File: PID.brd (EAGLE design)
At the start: 160 x 100 mm, 11 parts, among them IC1 UA741CPE4, IC2 UA741CPE4, IC3 UA741CPE4

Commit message: paf
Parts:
- added CONSIGNE, RETOUR, RETOUR1: (no value), pinhead:1X01
- added IC4, IC5: UA741CPE4, SamacSys_Parts:DIP794W53P254L959H508Q8N
- added R1, R3, R4, R6: 22k, rcl:0204/7
- added R10, R7, R8, R9: 10k, rcl:0204/7
- added R11: 2.5k, rcl:0204/7
- added R5: (no value), rcl:0204/7
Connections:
- new net CONSIGNE: CONSIGNE.1, R4.1
- new net N$13: IC5.3, R4.2, R6.2
- new net N$15: IC4.2, R10.1, R7.2, R8.2, R9.2
- new net N$17: C3.+, R5.2
- new net N$18: IC4.3, R11.2
- new net N$9: IC5.2, R1.1, R3.2
- new net OUTPUT: IC4.6, R10.2, RETOUR1.1
- new net RETOUR: R3.1, R5.1, RETOUR.1
- net GND: now also R11.1, R6.1
- net N$10: now also R9.1
- net N$2: now also R7.1
- net N$4: now also R8.1
- net N$7: now also IC5.6, R1.2, R2.1
- net V+: now also IC4.7, IC5.7
- net V-: now also IC4.4, IC5.4

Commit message: paf
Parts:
- removed R5: (no value), rcl:0204/7
- removed VR1: T7YA103MT20, PFE:T7YA
- added R13, R14: 22k, rcl:0204/7
- R1, R3: value 22k -> (none)
- R11: value 2.5k -> 5k
- R2: value (none) -> T7YA103MT20; device rcl:0204/7 -> PFE:T7YA
- moved R1 112.5 mm to (-17.8, 22.9)
- moved R3 20.3 mm to (-30.5, -114.3)
- moved R2 9.92 mm to (-24.1, 15.2)
- renumbered C1 to CI1, C2 to CI2, C3 to CD1, C4 to CD2, VR2 to RI, VR3 to RD
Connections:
- new net N$16: IC4.2, R10.1, R7.2, R8.2
- net N$15: now also IC5.6, R13.2; no longer IC4.2, R10.1, R7.2, R8.2, R9.2
- net N$17: now also R3.2; no longer R5.2
- net N$18: now also R9.2
- net N$2: now also R2.C; no longer VR1.C
- net N$3: now also R1.2, R2.A, R2.B; no longer R2.2, VR1.A, VR1.B
- net N$7: now also R1.1; no longer IC5.6, R1.2, R2.1
- net N$9: now also R13.1, R14.2; no longer R1.1, R3.2
- net RETOUR: now also R14.1; no longer R5.1

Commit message: paf
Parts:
- renumbered RETOUR1 to OUTPUT
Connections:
- removed net N$7 (its old number): R1.1, RI.A, RI.B
- net N$15: now also R1.1, RI.A, RI.B
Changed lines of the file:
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@@
 <attribute name="VALUE" x="-32.1056" y="-156.6926" size="0.9906" layer="27" ratio="10"/>
 </element>
-<element name="RETOUR1" library="pinhead" library_urn="urn:adsk.eagle:library:325" package="1X01" package3d_urn="urn:adsk.eagle:package:22485/2" value="" x="-33.02" y="-161.29" smashed="yes">
+<element name="OUTPUT" library="pinhead" library_urn="urn:adsk.eagle:library:325" package="1X01" package3d_urn="urn:adsk.eagle:package:22485/2" value="" x="-33.02" y="-161.29" smashed="yes">
 <attribute name="NAME" x="-34.3662" y="-159.4612" size="1.27" layer="25" ratio="10"/>
 <attribute name="POPULARITY" value="64" x="-33.02" y="-161.29" size="1.778" layer="27" display="off"/>
@@
 <wire x1="-14.13" y1="-7.62" x2="-29.21" y2="-13.97" width="0" layer="19" extent="1-1"/>
 </signal>
-<signal name="N$7">
-<contactref element="RI" pad="A"/>
-<contactref element="RI" pad="B"/>
-<contactref element="R1" pad="1"/>
-<wire x1="-31.75" y1="-16.51" x2="-29.21" y2="-19.05" width="0" layer="19" extent="1-1"/>
-<wire x1="-21.59" y1="22.86" x2="-31.75" y2="-16.51" width="0" layer="19" extent="1-1"/>
-</signal>
 <signal name="N$8">
 <contactref element="CI1" pad="-"/>
@@
 <contactref element="IC4" pad="6"/>
 <contactref element="R10" pad="2"/>
-<contactref element="RETOUR1" pad="1"/>
+<contactref element="OUTPUT" pad="1"/>
 <wire x1="-26.67" y1="-151.13" x2="-33.02" y2="-161.29" width="0" layer="19" extent="1-1"/>
 <wire x1="-25.24" y1="-143.51" x2="-26.67" y2="-151.13" width="0" layer="19" extent="1-1"/>
@@
 <wire x1="-26.67" y1="-134.62" x2="-33.18" y2="-143.51" width="0" layer="19" extent="1-1"/>
 </signal>
-<signal name="N$16">
+<signal name="N$15">
+<contactref element="IC5" pad="6"/>
+<contactref element="R13" pad="2"/>
+<contactref element="RI" pad="A"/>
+<contactref element="RI" pad="B"/>
+<contactref element="R1" pad="1"/>
+<wire x1="-25.24" y1="-81.28" x2="-26.67" y2="-88.9" width="0" layer="19" extent="1-1"/>
+<wire x1="-29.21" y1="-19.05" x2="-25.24" y2="-81.28" width="0" layer="19" extent="1-1"/>
+<wire x1="-31.75" y1="-16.51" x2="-29.21" y2="-19.05" width="0" layer="19" extent="1-1"/>
+<wire x1="-21.59" y1="22.86" x2="-31.75" y2="-16.51" width="0" layer="19" extent="1-1"/>
+</signal>
+<signal name="N$7">
 <contactref element="R8" pad="2"/>
 <contactref element="R7" pad="2"/>
@@
 <wire x1="-26.67" y1="-124.46" x2="-26.67" y2="-129.54" width="0" layer="19" extent="1-1"/>
 </signal>
-<signal name="N$15">
-<contactref element="IC5" pad="6"/>
-<contactref element="R13" pad="2"/>
-<wire x1="-25.24" y1="-81.28" x2="-26.67" y2="-88.9" width="0" layer="19" extent="1-1"/>
-</signal>
 </signals>

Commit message: paf
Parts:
- moved CI1 1.27 mm to (-33.0, -24.1)
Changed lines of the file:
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@@
 <attribute name="VALUE" x="-29.493" y="-16.535" size="1.27" layer="27" align="center"/>
 </element>
-<element name="CI1" library="rcl" library_urn="urn:adsk.eagle:library:334" package="E2,5-6" package3d_urn="urn:adsk.eagle:package:23349/1" value="" x="-33.02" y="-25.4" smashed="yes">
-<attribute name="NAME" x="-30.353" y="-23.876" size="1.27" layer="25" ratio="10"/>
-<attribute name="POPULARITY" value="26" x="-33.02" y="-25.4" size="1.778" layer="27" display="off"/>
-<attribute name="SPICEPREFIX" value="C" x="-33.02" y="-25.4" size="1.778" layer="27" display="off"/>
-<attribute name="VALUE" x="-30.353" y="-28.067" size="1.27" layer="27" ratio="10"/>
+<element name="CI1" library="rcl" library_urn="urn:adsk.eagle:library:334" package="E2,5-6" package3d_urn="urn:adsk.eagle:package:23349/1" value="" x="-33.02" y="-24.13" smashed="yes">
+<attribute name="NAME" x="-30.353" y="-22.606" size="1.27" layer="25" ratio="10"/>
+<attribute name="POPULARITY" value="26" x="-33.02" y="-24.13" size="1.778" layer="27" display="off"/>
+<attribute name="SPICEPREFIX" value="C" x="-33.02" y="-24.13" size="1.778" layer="27" display="off"/>
+<attribute name="VALUE" x="-30.353" y="-26.797" size="1.27" layer="27" ratio="10"/>
 </element>
 <element name="CI2" library="rcl" library_urn="urn:adsk.eagle:library:334" package="E2,5-6" package3d_urn="urn:adsk.eagle:package:23349/1" value="" x="-33.02" y="-31.75" smashed="yes">
@@
 <contactref element="RI" pad="C"/>
 <contactref element="CI1" pad="+"/>
-<wire x1="-29.21" y1="-13.97" x2="-34.29" y2="-25.4" width="0" layer="19" extent="1-1"/>
+<wire x1="-29.21" y1="-13.97" x2="-34.29" y2="-24.13" width="0" layer="19" extent="1-1"/>
 <wire x1="-14.13" y1="-7.62" x2="-29.21" y2="-13.97" width="0" layer="19" extent="1-1"/>
 </signal>
@@
 <contactref element="CI1" pad="-"/>
 <contactref element="CI2" pad="-"/>
-<wire x1="-31.75" y1="-25.4" x2="-31.75" y2="-31.75" width="0" layer="19" extent="1-1"/>
+<wire x1="-31.75" y1="-24.13" x2="-31.75" y2="-31.75" width="0" layer="19" extent="1-1"/>
 </signal>
 <signal name="N$10">

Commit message: paf
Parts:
- removed R1, R3: (no value), rcl:0204/7
- removed R2: T7YA103MT20, PFE:T7YA
- added GND, V+, V-: (no value), pinhead:1X01
- added RD1, RP1: (no value), rcl:0204/7
- added RP: T7YA103MT20, PFE:T7YA
- added S1, S2, S3: TL36PO, switch:TL3XPO
- moved R10 197.1 mm to (57.1, 25.4)
- moved OUTPUT 190.4 mm to (57.1, 6.35)
- moved R11 188.6 mm to (58.4, 10.2)
- moved IC4 182.4 mm to (58.4, 17.8)
- moved R7 173.8 mm to (50.8, 29.2), turned to 270 degrees
- moved R8 169.4 mm to (50.8, 19.1), turned to 90 degrees
- moved R9 164.9 mm to (50.8, 8.89), turned to 90 degrees
- moved R6 148.8 mm to (8.89, 24.1), turned to 180 degrees
- moved RETOUR 148.6 mm to (10.2, 33.0), turned to 270 degrees
- moved CONSIGNE 143.1 mm to (7.62, 33.0), turned to 270 degrees
- moved R4 134.2 mm to (8.89, 29.2), turned to 180 degrees
- moved R14 126.9 mm to (8.89, 26.7), turned to 180 degrees
- moved R13 105.4 mm to (8.89, 8.89)
- moved IC5 103.8 mm to (8.89, 16.5)
- moved CD1 89.0 mm to (26.7, 6.35), turned to 90 degrees
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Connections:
- new net N$12: R7.1, S1.2
- new net N$16: R8.1, S2.2
- new net N$19: R9.1, S3.2
- net GND: now also GND.1, S1.1, S2.1, S3.1
- net N$10: now also S3.3; no longer R9.1
- net N$15: now also RP1.1; no longer R1.1
- net N$17: now also RD1.2; no longer R3.2
- net N$2: now also RP.C, S1.3; no longer R2.C, R7.1
- net N$3: now also RP.A, RP.B, RP1.2; no longer R1.2, R2.A, R2.B
- net N$4: now also S2.3; no longer R8.1
- net RETOUR: now also RD1.1; no longer R3.1
- net V+: now also V+.1
- net V-: now also V-.1
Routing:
- net V-: track 0.00 -> 136.0 mm
- net GND: track 0.00 -> 121.4 mm
- net V+: track 0.00 -> 109.3 mm
- net N$2: track 0.00 -> 38.8 mm
- net N$10: track 0.00 -> 35.4 mm
- net N$15: track 0.00 -> 33.5 mm
- net RETOUR: track 0.00 -> 31.3 mm
- net OUTPUT: track 0.00 -> 23.4 mm
- net N$4: track 0.00 -> 22.7 mm
- net N$9: track 0.00 -> 21.9 mm
- net N$11: track 0.00 -> 18.8 mm
- net N$13: track 0.00 -> 18.7 mm
- net N$18: track 0.00 -> 18.6 mm
- net N$3: track 0.00 -> 17.7 mm
- net N$17: track 0.00 -> 14.5 mm
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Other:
- board size 160 x 100 mm -> 67.3 x 40.3 mm

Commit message: couocu
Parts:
- removed S1, S2, S3: TL36PO, switch:TL3XPO
- added JP1, JP2, JP3: (no value), pinhead:1X02
- added R1: 100k, rcl:0204/7
- moved RP1 2.54 mm to (16.5, 33.0)
- moved IC4 1.80 mm to (57.1, 19.1)
- moved GND 1.80 mm to (55.9, 33.0)
- moved V- 1.80 mm to (53.3, 35.6)
- moved R7 1.80 mm to (49.5, 30.5)
- moved R8 1.80 mm to (49.5, 20.3)
- moved R9 1.80 mm to (49.5, 10.2)
- moved V+ 1.80 mm to (58.4, 30.5)
- moved R10 1.27 mm to (57.1, 26.7)
- moved R11 1.27 mm to (57.1, 10.2)
- moved CONSIGNE 1.27 mm to (6.35, 33.0)
- moved IC5 1.27 mm to (7.62, 16.5)
- moved R13 1.27 mm to (7.62, 8.89)
- moved R14 1.27 mm to (7.62, 26.7)
- moved R4 1.27 mm to (7.62, 29.2)
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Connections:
- net N$15 renamed ERREUR
- net GND: no longer S1.1, S2.1, S3.1
- net N$10: now also JP3.1; no longer S3.3
- net N$12: now also JP1.2; no longer S1.2
- net N$16: now also JP2.2; no longer S2.2
- net N$19: now also JP3.2; no longer S3.2
- net N$2: now also JP1.1; no longer S1.3
- net N$4: now also JP2.1, R1.2; no longer S2.3
- net N$5: now also R1.1
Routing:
- net V-: track 136.0 -> 111.5 mm
- net N$5: track 11.6 -> 27.6 mm
- net V+: track 109.3 -> 101.7 mm
- net N$10: track 35.4 -> 28.5 mm
- net N$4: track 22.7 -> 26.8 mm
- net N$2: track 38.8 -> 34.8 mm
- net N$3: track 17.7 -> 20.5 mm
- net N$18: track 18.6 -> 16.3 mm
- net N$16: track 7.81 -> 6.13 mm
- net N$9: track 21.9 -> 23.6 mm
- net N$19: track 6.66 -> 5.08 mm
- net N$7: track 10.6 -> 11.9 mm
- net N$11: track 18.8 -> 20.0 mm
- net N$17: track 14.5 -> 15.8 mm
- net ERREUR: track 33.5 -> 32.4 mm
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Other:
- board size 67.3 x 40.3 mm -> 70 x 44 mm
- board text added: "PID board alpha DX+"

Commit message: paf
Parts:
- added R2: 1k, rcl:0204/7
- CD1, CD2: value (none) -> 10µ
- CI1, CI2: value (none) -> 470µ
- RD, RP: value T7YA103MT20 -> 10k
- RD1: value (none) -> 200
- RI: value T7YA103MT20 -> 100k
- RP1: value (none) -> 1k
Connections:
- new net N$15: R2.2, RI.A, RI.B
- net ERREUR: now also R2.1; no longer RI.A, RI.B
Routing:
- net GND: track 121.1 -> 0.00 mm
- net V-: track 111.5 -> 0.00 mm
- net V+: track 101.7 -> 0.00 mm
- net N$2: track 34.8 -> 0.00 mm
- net ERREUR: track 32.4 -> 0.00 mm
- net RETOUR: track 31.9 -> 0.00 mm
- net N$10: track 28.5 -> 0.00 mm
- net N$5: track 27.6 -> 0.00 mm
- net N$4: track 26.8 -> 0.00 mm
- net OUTPUT: track 24.4 -> 0.00 mm
- net N$9: track 23.6 -> 0.00 mm
- net N$3: track 20.5 -> 0.00 mm
- net N$11: track 20.0 -> 0.00 mm
- net N$13: track 18.6 -> 0.00 mm
- net N$18: track 16.3 -> 0.00 mm
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
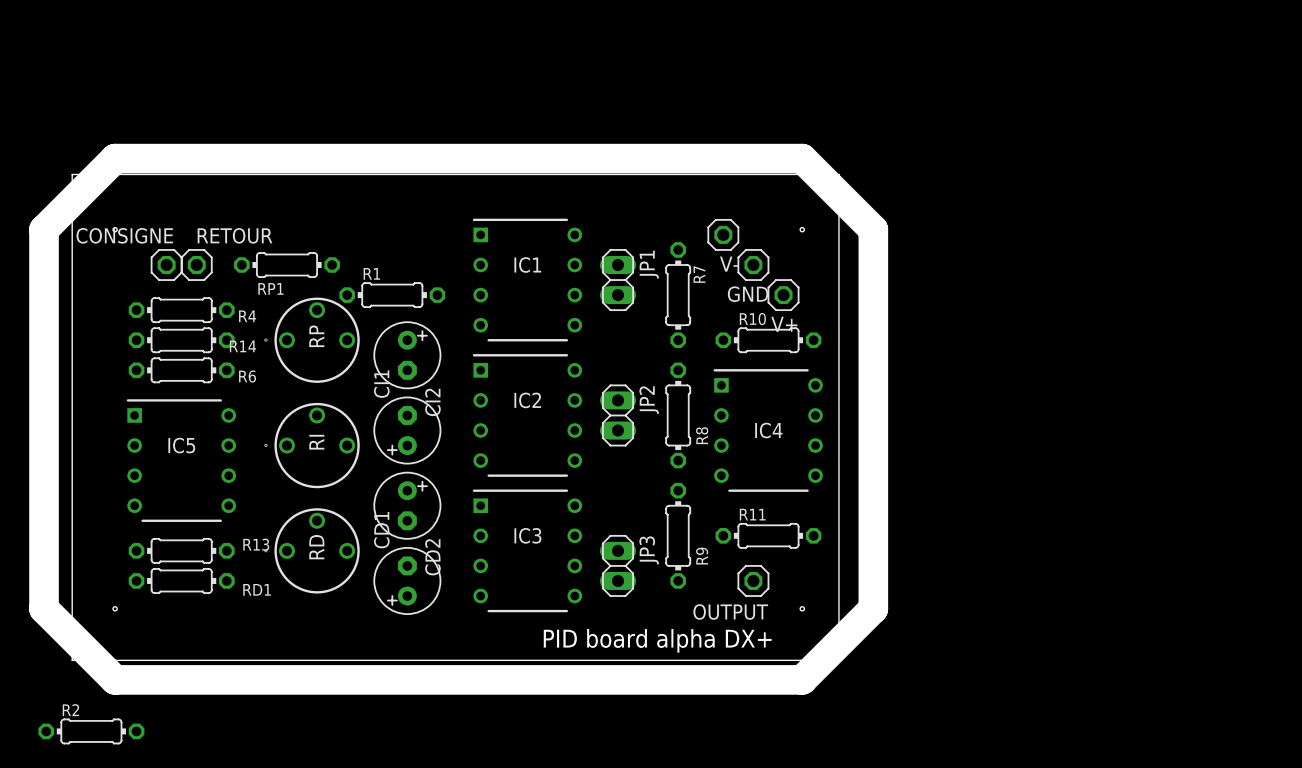
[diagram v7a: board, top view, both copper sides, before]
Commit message: Le routage de lavage, tous les signaux sur le bottom, le plan de masse sur le bottom, plan de V- sur le top et routage du V+ sur le top
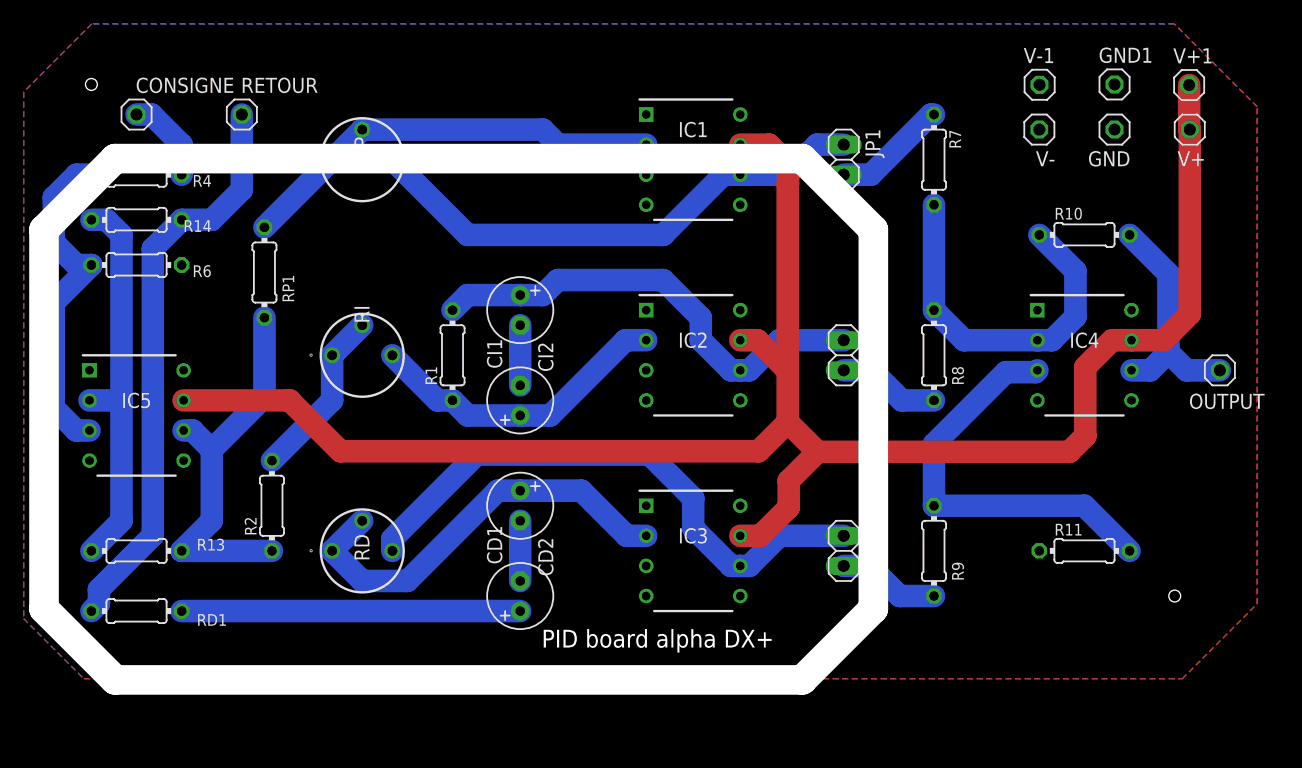
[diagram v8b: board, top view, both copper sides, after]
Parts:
- added GND1, V+1, V-1: (no value), pinhead:1X01
- moved OUTPUT 43.2 mm to (95.2, 24.1)
- moved V+ 37.0 mm to (92.7, 44.5)
- moved GND 32.6 mm to (86.4, 44.5)
- moved V- 28.1 mm to (80.0, 44.5)
- moved R10 28.1 mm to (83.8, 35.6)
- moved IC4 27.4 mm to (83.8, 25.4)
- moved R11 26.7 mm to (83.8, 8.89)
- moved R7 24.4 mm to (71.1, 41.9)
- moved R2 24.4 mm to (15.2, 12.7), turned to 90 degrees
- moved R8 22.2 mm to (71.1, 25.4)
- moved R9 21.6 mm to (71.1, 8.89)
- moved JP1 21.6 mm to (63.5, 41.9)
- moved JP2 19.7 mm to (63.5, 25.4)
- moved JP3 19.1 mm to (63.5, 8.89)
- moved IC1 17.3 mm to (50.8, 41.9)
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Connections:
- net GND: now also GND1.1
- net V+: now also V+1.1
- net V-: now also V-1.1
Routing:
- net V+: track 0.00 -> 158.7 mm
- net RETOUR: track 0.00 -> 48.7 mm
- net N$10: track 0.00 -> 48.5 mm
- net N$2: track 0.00 -> 43.9 mm
- net N$4: track 0.00 -> 39.4 mm
- net N$3: track 0.00 -> 36.2 mm
- net N$11: track 0.00 -> 35.9 mm
- net N$18: track 0.00 -> 34.6 mm
- net N$9: track 0.00 -> 33.5 mm
- net ERREUR: track 0.00 -> 33.2 mm
- net N$7: track 0.00 -> 30.9 mm
- net N$13: track 0.00 -> 28.9 mm
- net N$17: track 0.00 -> 28.6 mm
- net N$5: track 0.00 -> 26.2 mm
- net OUTPUT: track 0.00 -> 20.0 mm
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- added copper zone on layer 1, net GND
- added copper zone on layer 16, net V-
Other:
- outline, holes or cut-outs redrawn
